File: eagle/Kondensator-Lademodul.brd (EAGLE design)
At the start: 71 x 64 mm, 24 parts, among them IC3 7818TV, X1 MKDSN1,5/2-5,08, X2 MKDSN1,5/2-5,08, X3 MKDSN1,5/2-5,08

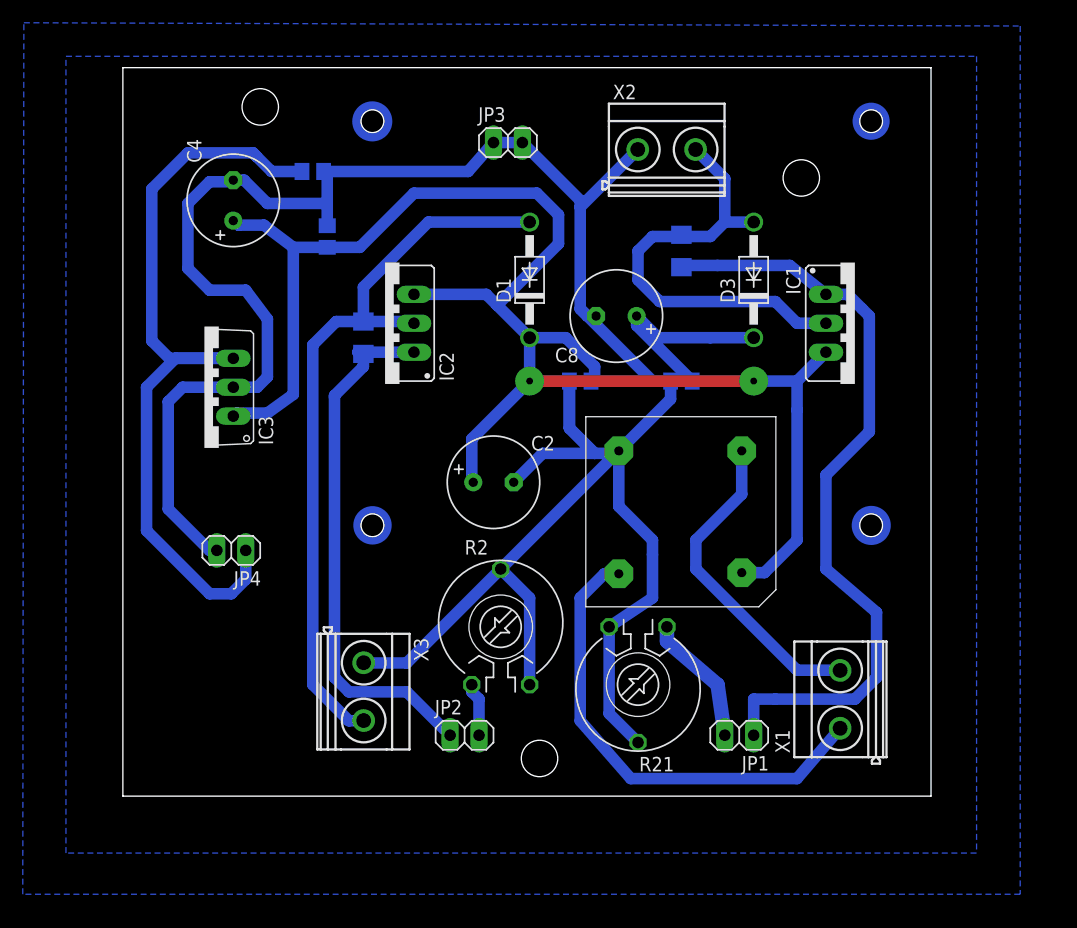
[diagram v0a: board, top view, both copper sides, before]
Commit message: Adjusted drill positions, little size corrections, new pin header
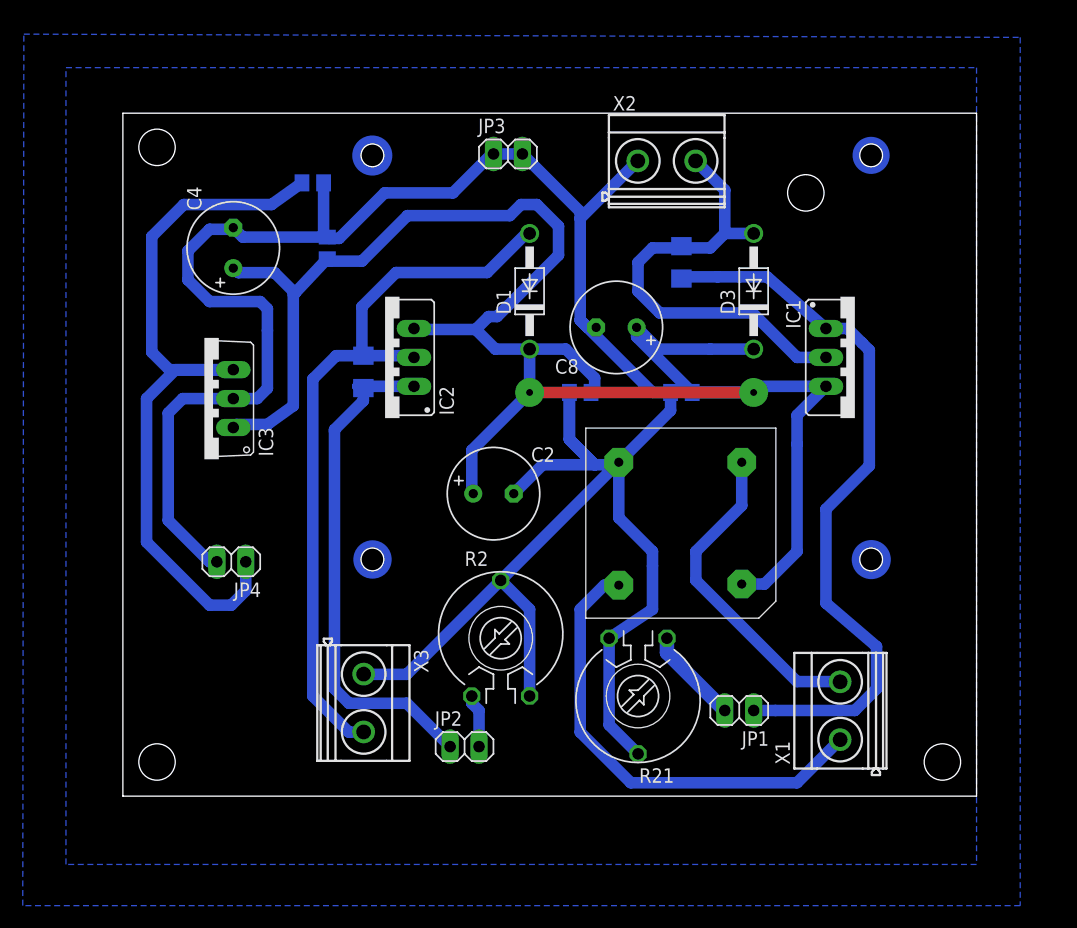
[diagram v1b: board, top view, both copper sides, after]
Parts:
- moved C4 4.18 mm to (9.70, 48.2)
- moved IC1 3.00 mm to (64.3, 38.5)
- moved IC2 3.00 mm to (23.0, 38.5)
- moved R1 3.00 mm to (21.1, 37.3)
- moved JP1 2.18 mm to (54.1, 7.53)
- moved C1 1.00 mm to (40.2, 35.5)
- moved C2 1.00 mm to (32.6, 26.6)
- moved C5 1.00 mm to (18.0, 48.2)
- moved C6 1.00 mm to (16.7, 53.9)
- moved C7 1.00 mm to (49.1, 35.5)
- moved C8 1.00 mm to (43.4, 41.2)
- moved D1 1.00 mm to (35.7, 44.4)
- moved D3 1.00 mm to (55.4, 44.4)
- moved IC3 1.00 mm to (7.16, 34.9)
- moved JP2 1.00 mm to (30.0, 4.35)
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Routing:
- net N$30: track 68.5 -> 64.1 mm
- net N$2: track 72.1 -> 68.3 mm
- net N$29: track 11.6 -> 8.45 mm
- net N$4: track 47.2 -> 45.2 mm
- net GND: track 222.4 -> 221.3 mm
- net N$25: track 42.2 -> 41.3 mm
- net N$17: track 172.6 -> 173.5 mm
- net N$28: track 39.4 -> 40.2 mm
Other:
- board size 71 x 64 mm -> 75 x 60 mm

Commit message: Fixed setup of capacitors (bigger and not in conflict)
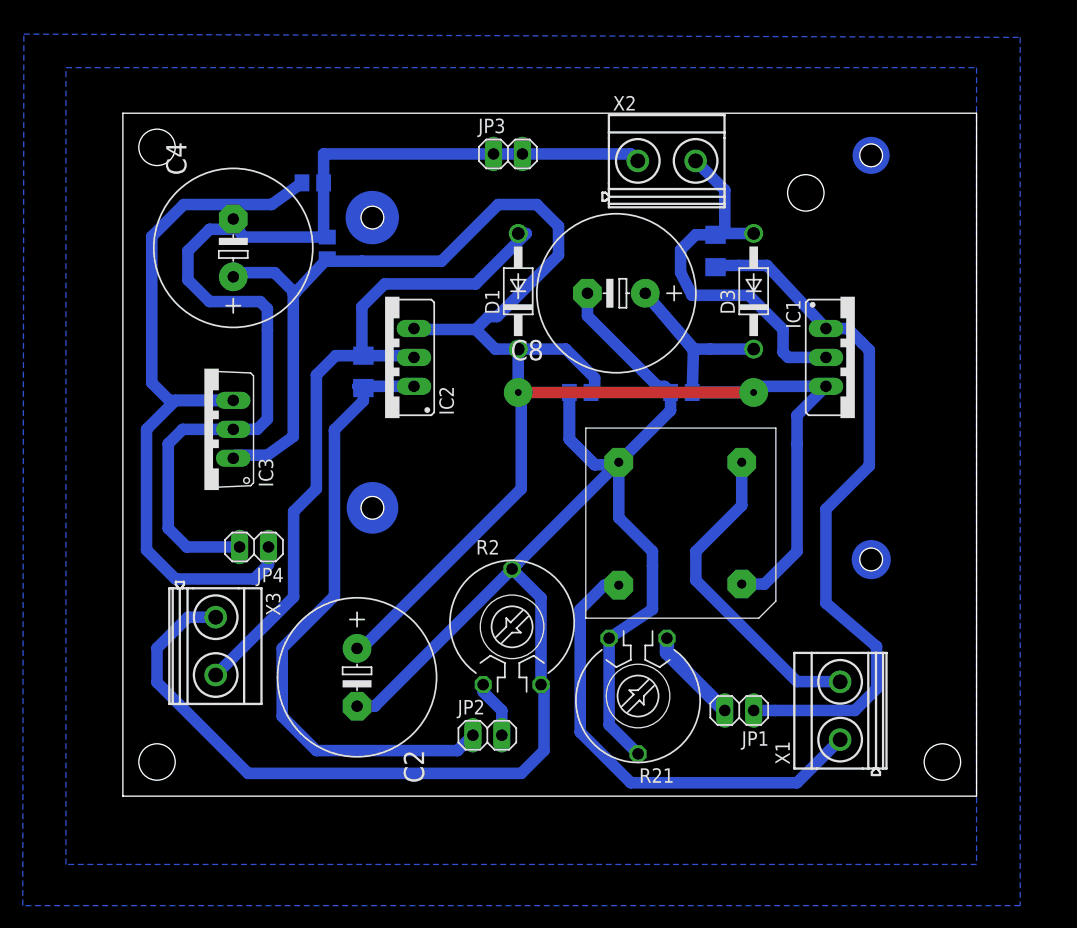
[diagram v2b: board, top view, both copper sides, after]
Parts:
- C2, C8: value 100µ -> 1000µ; device rcl:E3,5-8 -> rcl:E5-13
- C4: device rcl:E3,5-8 -> rcl:E5-13
- moved C2 20.1 mm to (20.6, 10.4), turned to 270 degrees
- moved X3 13.9 mm to (8.13, 13.2)
- moved R20 3.16 mm to (52.1, 47.9)
- moved C8 3.00 mm to (43.4, 44.2)
- moved IC3 2.70 mm to (7.16, 32.2)
- moved JP4 2.39 mm to (11.5, 21.9)
- moved JP2 2.24 mm to (32.0, 5.35)
- moved R2 1.41 mm to (34.2, 14.9)
- moved D1 1.00 mm to (34.7, 44.4)
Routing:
- net GND: track 221.3 -> 258.3 mm
- net N$17: track 173.5 -> 199.3 mm
- net N$4: track 45.2 -> 55.8 mm
- net N$28: track 40.2 -> 34.3 mm
- net N$3: track 65.2 -> 61.5 mm
- net N$30: track 64.1 -> 61.8 mm
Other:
- board text added: "24V ~ IN"
- board text added: "C Hi"
- board text added: "C low"
- board text added: "Poti Hi"
- board text added: "Poti low"
- board text removed: "36V ~ IN"
- board text removed: "Poti V1"
- board text removed: "Poti V2"
- board text removed: "Widerstandskaskade 1"
- board text removed: "Widerstandskaskade 2"

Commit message: Var. Changes. Layout and new diode for 7818
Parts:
- added D2: 1N4004, diode:DO41-10
- added JP5: (no value), pinhead:1X02
- moved JP4 1.40 mm to (10.2, 21.6), turned to 90 degrees
- moved X3 1.00 mm to (8.13, 12.2)
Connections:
- net N$17: now also D2.C
- net N$2: now also D2.A, JP5.1
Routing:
- net N$17: track 199.3 -> 202.6 mm
- net GND: track 258.3 -> 256.6 mm
- net N$2: track 68.7 -> 69.6 mm
- net N$3: track 61.5 -> 62.3 mm

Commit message: Updated wrong resistor value
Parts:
- R1, R20: value 100k -> 120
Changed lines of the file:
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@@
 <element name="C8" library="rcl" package="E5-13" value="1000µ" x="43.355" y="44.18" rot="R180"/>
 <element name="D3" library="diode" package="DO41-10" value="1N4004" x="55.42" y="44.355" rot="R90"/>
-<element name="R20" library="rcl" package="R1206" value="100k" x="52.07" y="47.895" rot="MR90"/>
+<element name="R20" library="rcl" package="R1206" value="120" x="52.07" y="47.895" rot="MR90"/>
 <element name="R21" library="pot" package="PT-10" value="" x="45.26" y="8.795" rot="R180"/>
 <element name="JP1" library="pinhead" package="1X02" value="" x="54.15" y="7.525" rot="R180"/>
@@
 <element name="C2" library="rcl" package="E5-13" value="1000µ" x="20.575" y="10.44" rot="R270"/>
 <element name="D1" library="diode" package="DO41-10" value="1N4004" x="34.735" y="44.355" rot="R90"/>
-<element name="R1" library="rcl" package="R1206" value="100k" x="21.13" y="37.275" rot="MR90"/>
+<element name="R1" library="rcl" package="R1206" value="120" x="21.13" y="37.275" rot="MR90"/>
 <element name="R2" library="pot" package="PT-10" value="" x="34.195" y="14.875"/>
 <element name="JP2" library="pinhead" package="1X02" value="" x="32.02" y="5.35"/>

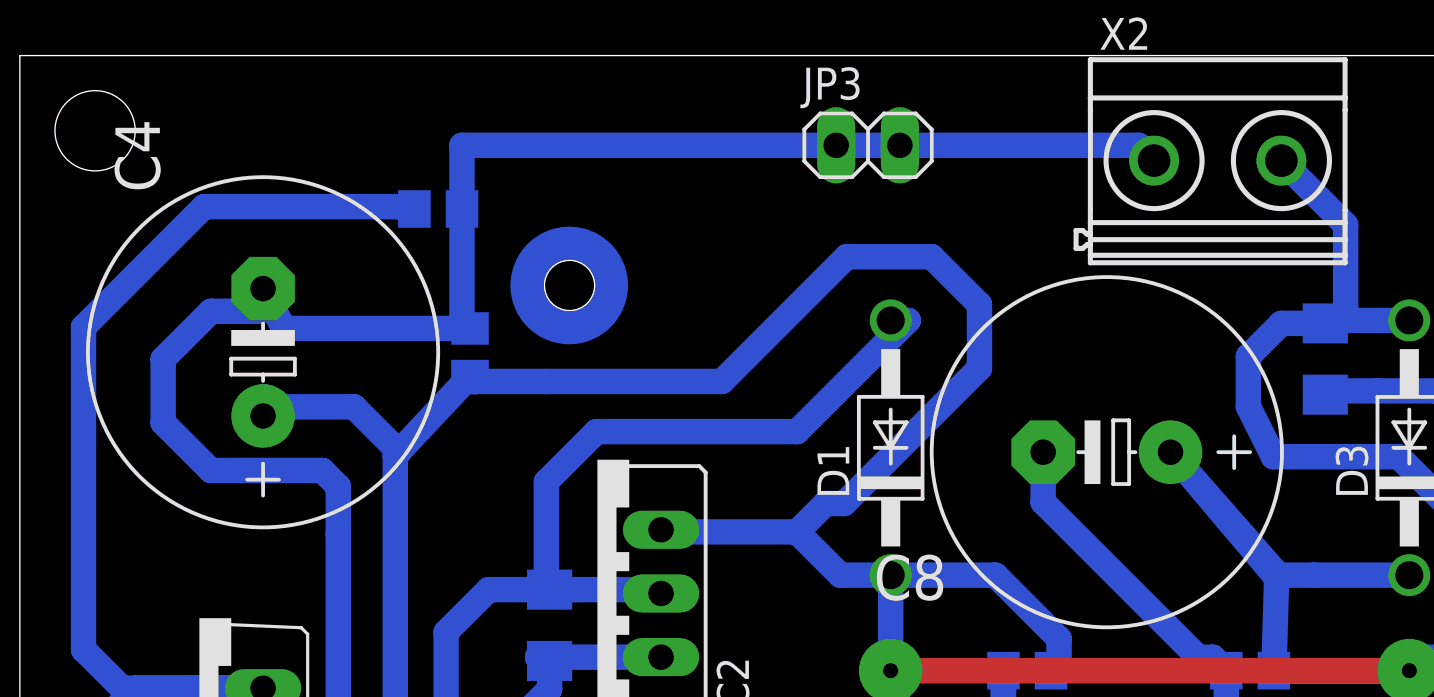
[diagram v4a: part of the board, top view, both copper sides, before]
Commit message: Added 'Gesamtschaltplan'
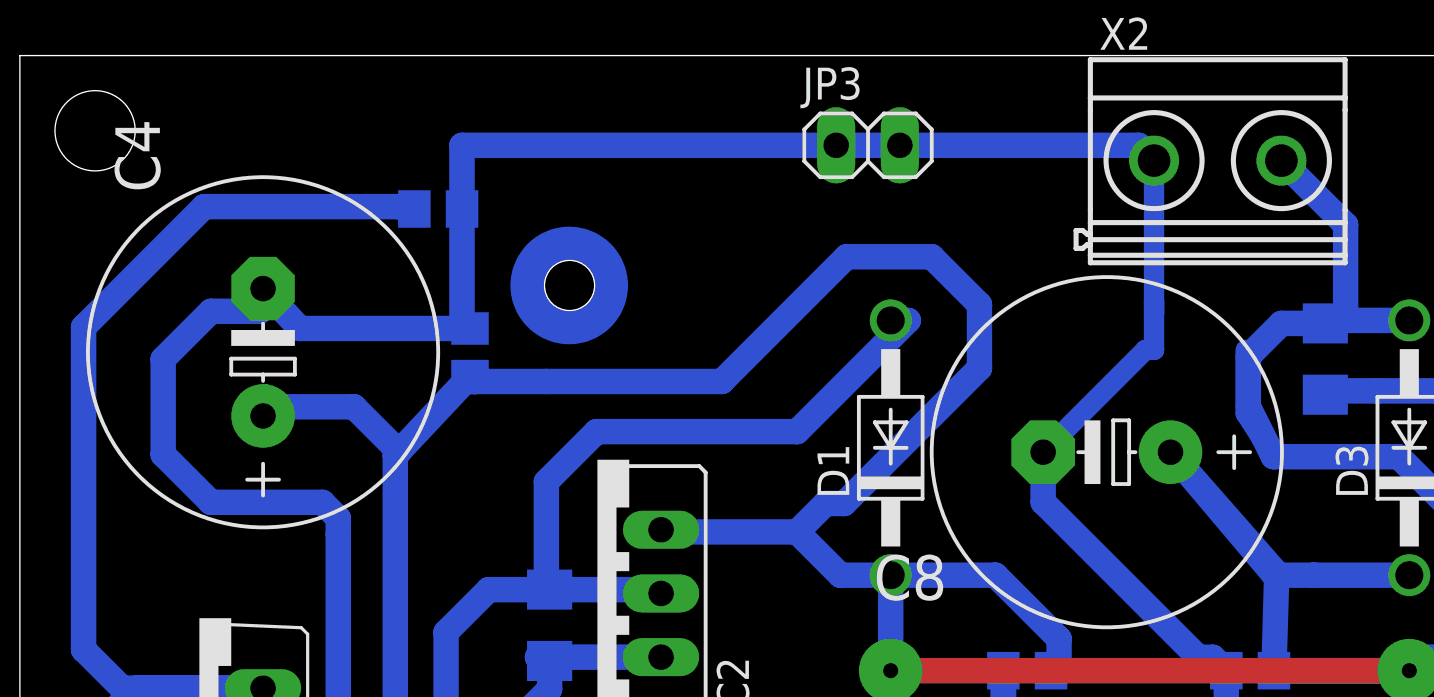
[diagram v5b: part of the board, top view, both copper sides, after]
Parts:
- R1, R20: value 120 -> 180
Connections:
- net GND: now also JP5.2
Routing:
- net GND: track 256.6 -> 270.5 mm
- net N$28: track 34.3 -> 38.9 mm
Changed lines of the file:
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@@
 <element name="C8" library="rcl" package="E5-13" value="1000µ" x="43.355" y="44.18" rot="R180"/>
 <element name="D3" library="diode" package="DO41-10" value="1N4004" x="55.42" y="44.355" rot="R90"/>
-<element name="R20" library="rcl" package="R1206" value="120" x="52.07" y="47.895" rot="MR90"/>
+<element name="R20" library="rcl" package="R1206" value="180" x="52.07" y="47.895" rot="MR90"/>
 <element name="R21" library="pot" package="PT-10" value="" x="45.26" y="8.795" rot="R180"/>
 <element name="JP1" library="pinhead" package="1X02" value="" x="54.15" y="7.525" rot="R180"/>
@@
 <element name="C2" library="rcl" package="E5-13" value="1000µ" x="20.575" y="10.44" rot="R270"/>
 <element name="D1" library="diode" package="DO41-10" value="1N4004" x="34.735" y="44.355" rot="R90"/>
-<element name="R1" library="rcl" package="R1206" value="120" x="21.13" y="37.275" rot="MR90"/>
+<element name="R1" library="rcl" package="R1206" value="180" x="21.13" y="37.275" rot="MR90"/>
 <element name="R2" library="pot" package="PT-10" value="" x="34.195" y="14.875"/>
 <element name="JP2" library="pinhead" package="1X02" value="" x="32.02" y="5.35"/>
@@
 <wire x1="11.795" y1="32.225" x2="12.7" y2="33.13" width="1.016" layer="16"/>
 <wire x1="12.7" y1="33.13" x2="12.7" y2="40.91" width="1.016" layer="16"/>
-<wire x1="7.62" y1="43.45" x2="5.715" y2="45.355" width="1.016" layer="16"/>
-<wire x1="5.715" y1="45.355" x2="5.715" y2="47.895" width="1.016" layer="16"/>
+<wire x1="7.62" y1="42.18" x2="5.715" y2="44.085" width="1.016" layer="16"/>
+<wire x1="5.715" y1="44.085" x2="5.715" y2="47.895" width="1.016" layer="16"/>
 <wire x1="5.715" y1="47.895" x2="7.62" y2="49.8" width="1.016" layer="16"/>
 <wire x1="7.62" y1="49.8" x2="9.557" y2="49.8" width="1.016" layer="16"/>
@@
 <wire x1="3.985" y1="30.955" x2="3.985" y2="24.525" width="1.016" layer="16"/>
 <wire x1="3.985" y1="24.525" x2="5.62" y2="22.89" width="1.016" layer="16"/>
-<wire x1="12.7" y1="40.91" x2="12.7" y2="42.815" width="1.016" layer="16"/>
-<wire x1="12.7" y1="42.815" x2="12.065" y2="43.45" width="1.016" layer="16"/>
-<wire x1="12.065" y1="43.45" x2="7.62" y2="43.45" width="1.016" layer="16"/>
+<wire x1="12.7" y1="40.91" x2="12.7" y2="41.545" width="1.016" layer="16"/>
+<wire x1="12.7" y1="41.545" x2="12.065" y2="42.18" width="1.016" layer="16"/>
+<wire x1="12.065" y1="42.18" x2="7.62" y2="42.18" width="1.016" layer="16"/>
 <wire x1="17.635" y1="53.88" x2="17.635" y2="49.435" width="1.016" layer="16"/>
 <wire x1="17.635" y1="49.435" x2="17.955" y2="49.115" width="1.016" layer="16"/>
-<wire x1="17.955" y1="49.115" x2="10.528" y2="49.115" width="1.016" layer="16"/>
-<wire x1="10.528" y1="49.115" x2="9.7" y2="50.705" width="1.016" layer="16"/>
+<wire x1="17.955" y1="49.115" x2="11.163" y2="49.115" width="1.016" layer="16"/>
+<wire x1="11.163" y1="49.115" x2="9.7" y2="50.705" width="1.016" layer="16"/>
 <wire x1="32.56" y1="56.42" x2="32.42" y2="56.42" width="1.016" layer="16"/>
 <wire x1="18.07" y1="49" x2="17.955" y2="49.115" width="1.016" layer="16"/>
@@
 <wire x1="5.62" y1="22.89" x2="10.19" y2="22.89" width="1.016" layer="16"/>
 <wire x1="10.19" y1="22.89" x2="10.16" y2="22.86" width="1.016" layer="16"/>
+<wire x1="44.895" y1="48.26" x2="40.815" y2="44.18" width="0.8128" layer="16"/>
+<wire x1="45.2389" y1="55.81" x2="45.2389" y2="50.165" width="0.8128" layer="16"/>
+<contactref element="JP5" pad="2"/>
+<wire x1="45.2389" y1="50.165" x2="45.2389" y2="49.6961" width="0.8128" layer="16"/>
+<wire x1="44.895" y1="48.26" x2="45.2389" y2="48.26" width="0.8128" layer="16"/>
+<wire x1="45.2389" y1="48.26" x2="45.2389" y2="50.165" width="0.8128" layer="16"/>
+<wire x1="5.62" y1="22.89" x2="6.35" y2="22.86" width="0" layer="19" extent="16-16"/>
 </signal>
 <signal name="N$24">
@@
 <wire x1="61.77" y1="38.545" x2="58.455" y2="38.545" width="1.016" layer="16"/>
 <wire x1="58.455" y1="38.545" x2="58" y2="39" width="1.016" layer="16"/>
+<wire x1="50" y1="44" x2="48.895" y2="45.72" width="0.8128" layer="16"/>
+<wire x1="48.895" y1="45.72" x2="48.895" y2="48.26" width="0.8128" layer="16"/>
 <wire x1="52.07" y1="49.317" x2="51.61" y2="49.165" width="0" layer="19" extent="16-16"/>
 </signal>
